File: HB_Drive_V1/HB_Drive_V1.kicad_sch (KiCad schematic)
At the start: 0 parts

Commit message: Adds Preliminary Hierarchical Schematics
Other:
- added sheet Current Monitor (CurrentMonitor.kicad_sch)
- added sheet Dead Time Injector (DeadTime.kicad_sch)
- added sheet Inner Current Regulator (IR.kicad_sch)
- added sheet Outer Voltage Regulator (VR.kicad_sch)
- added sheet PWM Comparator (Comparator.kicad_sch)
- added sheet Triangle Wave Generator (TriWaveGen.kicad_sch)

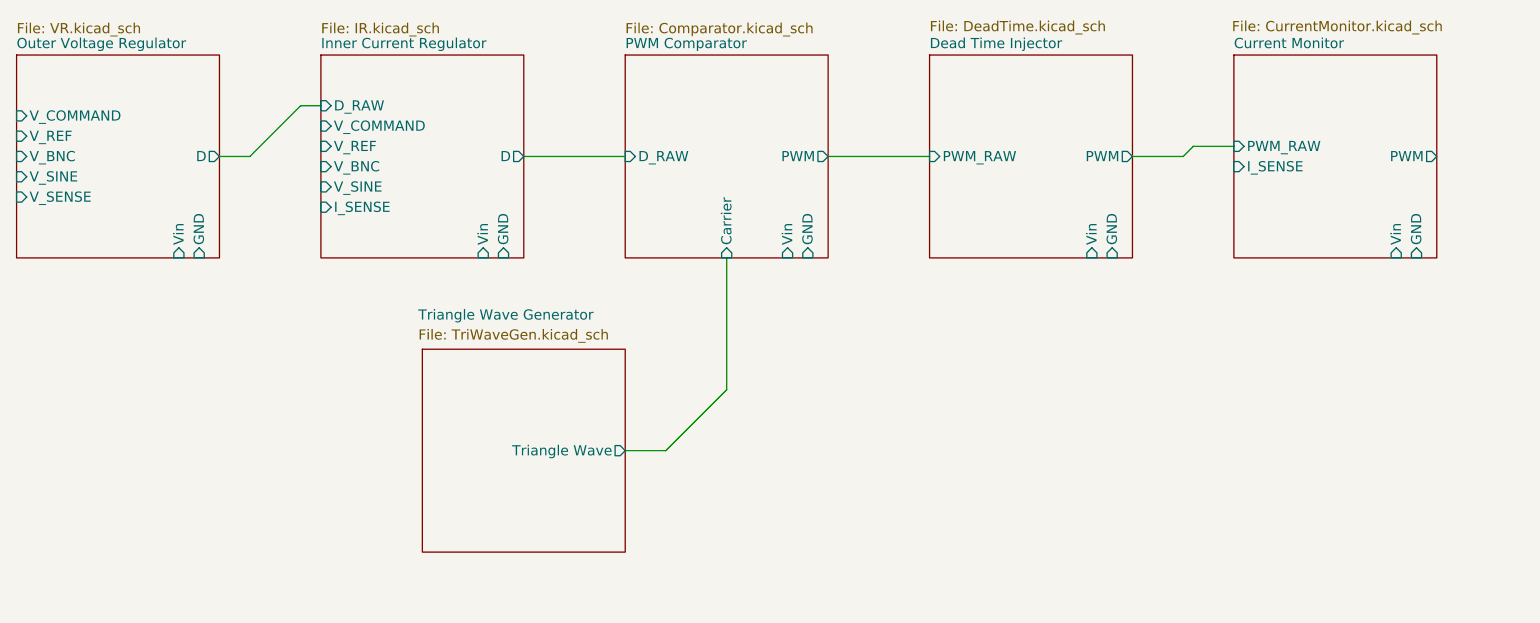
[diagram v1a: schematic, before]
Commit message: fixes git and adds a first revision of the Inner Current Regulator (NOT COMPLETE)
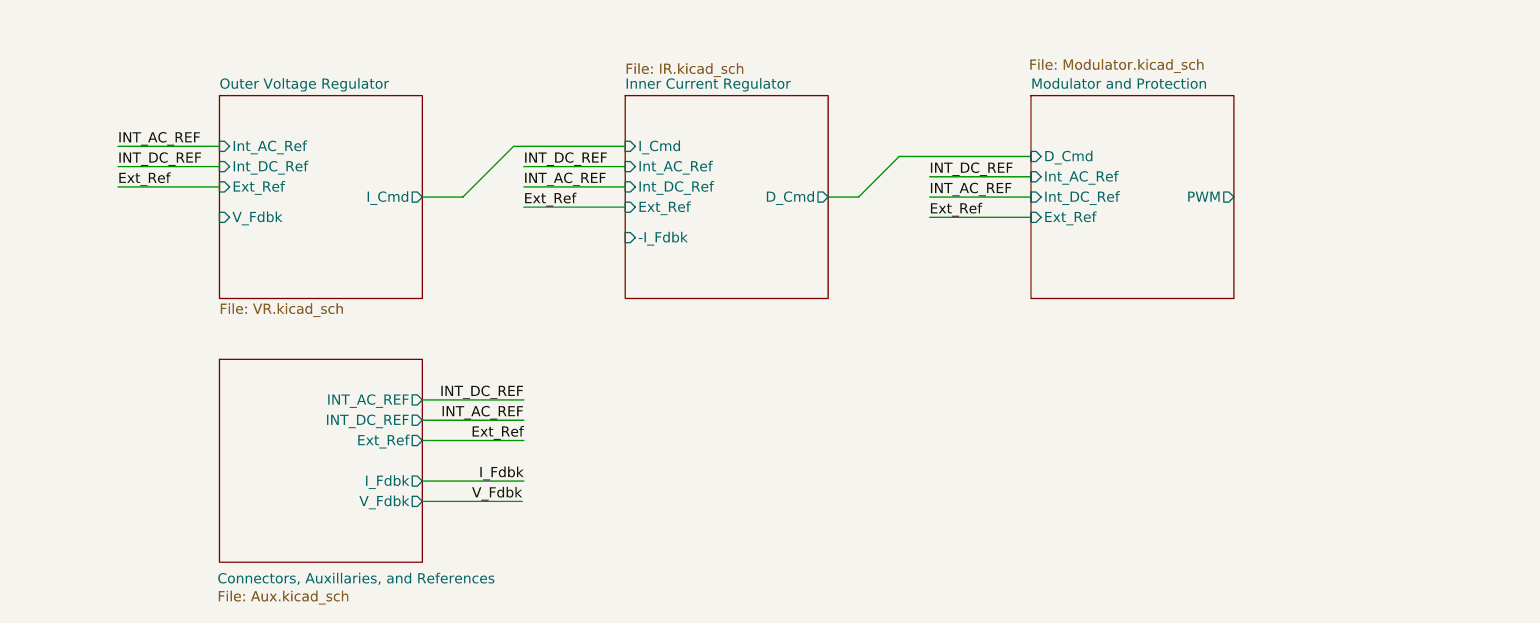
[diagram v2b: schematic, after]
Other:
- removed sheet Current Monitor
- removed sheet Dead Time Injector
- removed sheet PWM Comparator
- removed sheet Triangle Wave Generator
- added sheet Connectors, Auxillaries, and References (Aux.kicad_sch)
- added sheet Modulator and Protection (Modulator.kicad_sch)
- sheet Inner Current Regulator ports: added -I_Fdbk, D_Cmd, Ext_Ref, I_Cmd, Int_AC_Ref, Int_DC_Ref; removed D, D_RAW, GND, I_SENSE, V_BNC, V_COMMAND, V_REF, V_SINE, Vin
- sheet Outer Voltage Regulator ports: added Ext_Ref, I_Cmd, Int_AC_Ref, Int_DC_Ref, V_Fdbk; removed D, GND, V_BNC, V_COMMAND, V_REF, V_SENSE, V_SINE, Vin

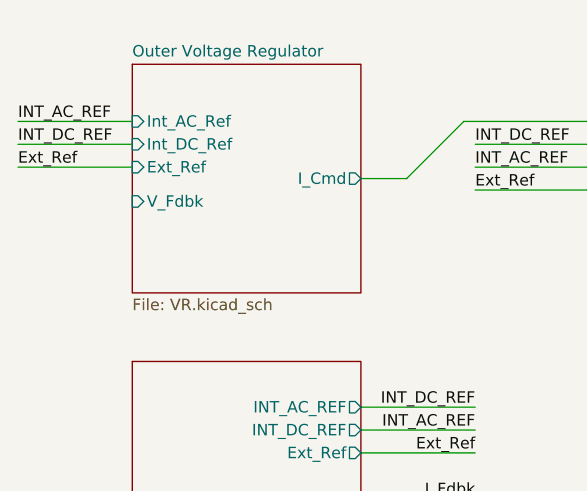
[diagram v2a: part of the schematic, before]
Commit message: adds 10v reference and DC offsets / gain control to I_fdbk and V_fdbk
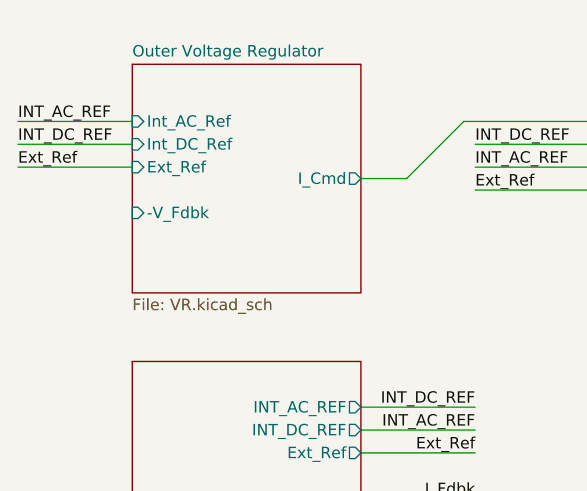
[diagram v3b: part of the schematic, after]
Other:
- sheet Outer Voltage Regulator ports: added -V_Fdbk; removed V_Fdbk
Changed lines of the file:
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@@
-			)
-		)
-		(pin "V_Fdbk" input
-			(at 88.9 83.82 180)
-			(effects
-				(font
-					(size 1.27 1.27)
-				)
-				(justify left)
 			)
 		)
@@
 			)
 		)
+		(pin "-V_Fdbk" input
+			(at 88.9 85.09 180)
+			(effects
+				(font
+					(size 1.27 1.27)
+				)
+				(justify left)
+			)
+		)
